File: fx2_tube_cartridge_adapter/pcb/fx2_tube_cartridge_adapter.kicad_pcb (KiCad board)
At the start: 2 copper layers, 56.5 x 53.5 mm, 3 parts

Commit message: Updated netlist as per hoglet's recommendations in http://www.stardot.org.uk/forums/viewtopic.php?f=3&t=13882&p=186963#p186908
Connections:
- CONN pad L8: (no net) -> cpu_CLK_jumper
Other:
- board text added: "- check that it's OK to have the lcsoft board below the flap in the plus 1 - consider ditching the tube interface, otherwise wire up 74hct00 and 74hct08 - check all TODO items in python netlist"
- board text added: "Electron cartridge / BBC Tube adapter for FX2 logic analyzer + decode6502 http://myelin.nz/acorn/fx2tube Copyright 2017 Google LLC Designed by Phillip Pearson"
- board text removed: "- check that it's OK to have the lcsoft board below the flap in the plus 1 - consider ditching the tube interface, otherwise wire up 74hct00 and 74hct08"
- board text removed: "Electron cartridge / BBC Tube adapter for FX2 logic analyzer + decode6502 Copyright 2017 Google LLC Designed by Phillip Pearson"
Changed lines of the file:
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@@
     (zones 0)
     (modules 3)
-    (nets 29)
+    (nets 30)
   )
   (page A4)
@@
   (net 27 cpu_nNMI)
   (net 28 cpu_SYNC)
+  (net 29 cpu_CLK_jumper)
   (net_class Default "This is the default net class."
     (clearance 0.1778)
@@
     (add_net cpu_A6)
     (add_net cpu_CLK)
+    (add_net cpu_CLK_jumper)
     (add_net cpu_D0)
     (add_net cpu_D1)
@@
     (pad L6 thru_hole circle (at 12.7 -2.54 90) (size 1.524 1.524) (drill 1.016) (layers *.Cu *.Mask)
       (net 2 GND))
-    (pad L8 thru_hole circle (at 12.7 0 90) (size 1.524 1.524) (drill 1.016) (layers *.Cu *.Mask))
+    (pad L8 thru_hole circle (at 12.7 0 90) (size 1.524 1.524) (drill 1.016) (layers *.Cu *.Mask)
+      (net 29 cpu_CLK_jumper))
     (pad L10 thru_hole circle (at 12.7 2.54 90) (size 1.524 1.524) (drill 1.016) (layers *.Cu *.Mask)
       (net 2 GND))
@@
       (net 2 GND))
   )
-  (gr_text "- check that it's OK\nto have the lcsoft\nboard below the flap\nin the plus 1\n\n- consider ditching\nthe tube interface,\notherwise wire up\n74hct00 and\n74hct08" (at 113.51 53.53) (layer F.Fab)
+  (gr_text "- check that it's OK\nto have the lcsoft\nboard below the flap\nin the plus 1\n\n- consider ditching\nthe tube interface,\notherwise wire up\n74hct00 and\n74hct08\n\n- check all TODO\nitems in python\nnetlist" (at 113.04 62.38) (layer F.Fab)
     (effects (font (size 1 1) (thickness 0.2)) (justify left))
   )
-  (gr_text "Electron cartridge / BBC Tube adapter\nfor FX2 logic analyzer + decode6502\n\nCopyright 2017 Google LLC\nDesigned by Phillip Pearson" (at 77.88 60.23) (layer B.SilkS)
+  (gr_text "Electron cartridge / BBC Tube adapter\nfor FX2 logic analyzer + decode6502\n\nhttp://myelin.nz/acorn/fx2tube\n\nCopyright 2017 Google LLC\nDesigned by Phillip Pearson" (at 77.88 60.23) (layer B.SilkS)
     (effects (font (size 1 1) (thickness 0.2)) (justify mirror))
   )

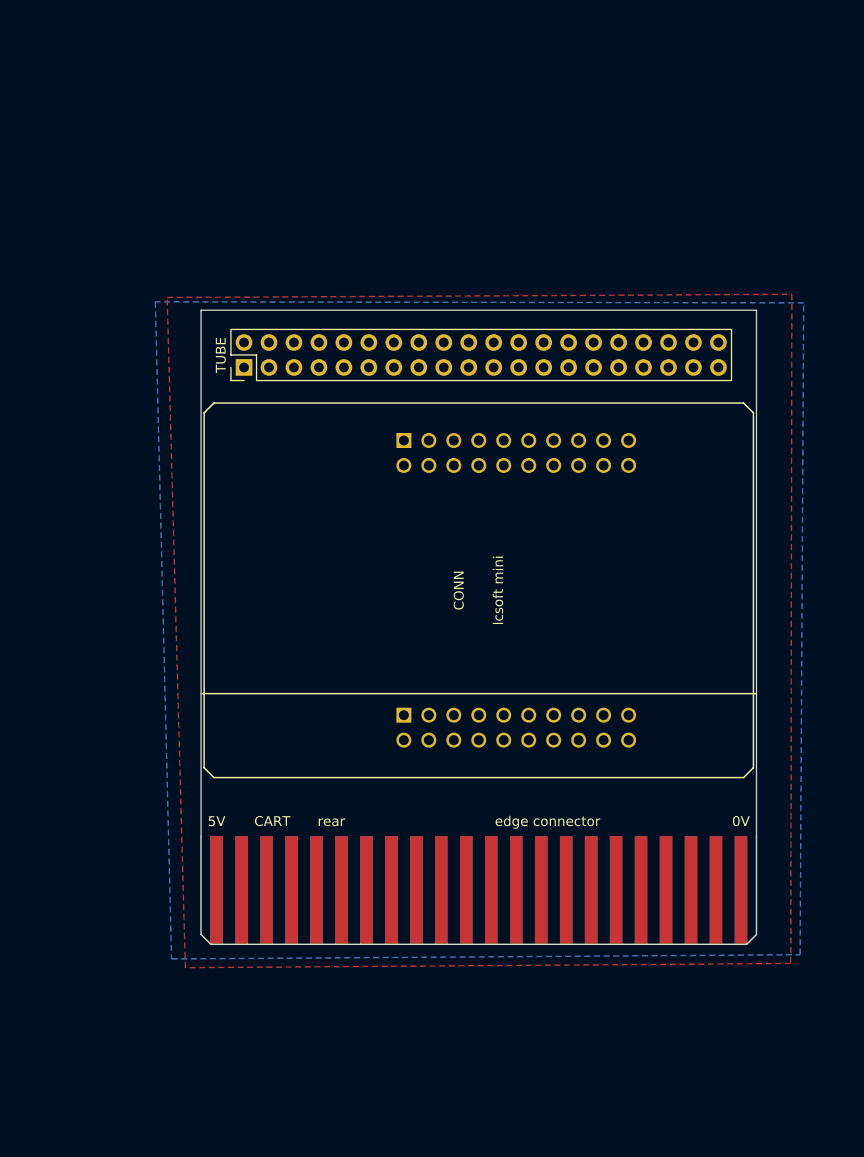
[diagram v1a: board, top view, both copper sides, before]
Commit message: fx2_tube_cartridge_adapter: routed cartridge to tube connections
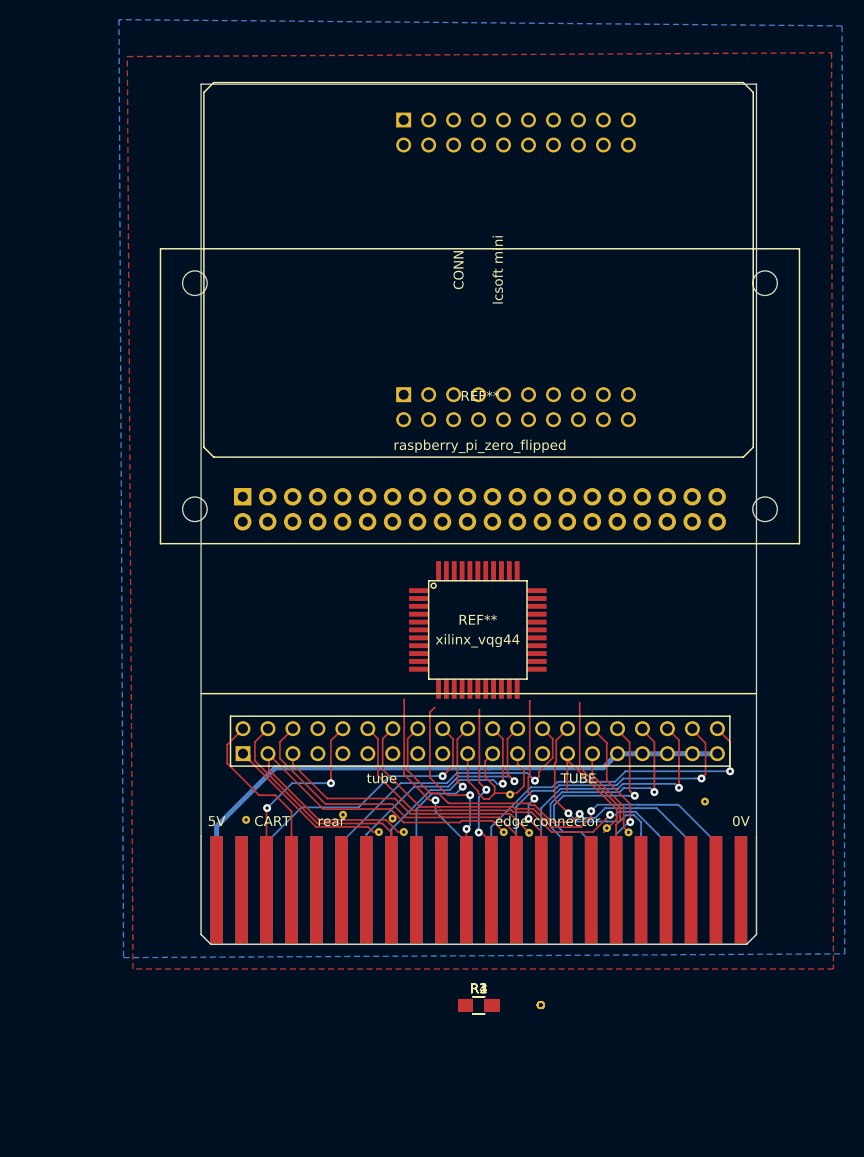
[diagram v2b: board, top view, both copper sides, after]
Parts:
- removed the TUBE at (55.1, 37.8)
- added R1, R2, R3, R4: 1k, Resistors_SMD:R_0805_HandSoldering, F.Cu at (79.0, 102.7)
- added REF**: raspberry_pi_zero_flipped, myelin-kicad:raspberry_pi_zero_flipped, F.Cu at (79.1, 55.7)
- added REF**: xilinx_vqg44, myelin-kicad:xilinx_vqg44, F.Cu at (78.9, 64.5)
- added TUBE: tube, myelin-kicad:header_2x20_100mil, F.Cu at (79.1, 75.8)
- added staple_single1: , myelin-kicad:via_single, F.Cu at (68.8, 85.1)
- added staple_single10: , myelin-kicad:via_single, F.Cu at (82.2, 81.3)
- added staple_single11: , myelin-kicad:via_single, F.Cu at (102.0, 82.0)
- added staple_single12, staple_single13, staple_single14, staple_single15, staple_single16, staple_single17, staple_single18, staple_single19, staple_single20: , myelin-kicad:via_single, F.Cu at (85.3, 102.7)
- added staple_single2: , myelin-kicad:via_single, F.Cu at (71.4, 85.1)
- added staple_single3: , myelin-kicad:via_single, F.Cu at (92.0, 84.7)
- added staple_single4: , myelin-kicad:via_single, F.Cu at (94.2, 85.1)
- added staple_single5: , myelin-kicad:via_single, F.Cu at (81.5, 85.1)
- added staple_single6: , myelin-kicad:via_single, F.Cu at (84.1, 85.2)
- added staple_single7: , myelin-kicad:via_single, F.Cu at (55.3, 83.8)
- added staple_single8: , myelin-kicad:via_single, F.Cu at (65.2, 83.3)
- added staple_single9: , myelin-kicad:via_single, F.Cu at (70.2, 83.7)
- moved CONN 32.6 mm to (79.0, 27.9)
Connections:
- CART pad B11: (no net) -> cpu_A7
- CONN pad R11: (no net) -> analyzer_PA2
- CONN pad R7: (no net) -> analyzer_PA6
- CONN pad R8: (no net) -> analyzer_PA5
- CONN pad R9: (no net) -> analyzer_PA4
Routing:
- net GND: track 0.00 -> 133.0 mm
- net 5V: track 0.00 -> 68.1 mm
- net cpu_D1: track 0.00 -> 48.6 mm, vias 0 -> 1
- net cpu_D0: track 0.00 -> 43.9 mm, vias 0 -> 1
- net cpu_D2: track 0.00 -> 42.9 mm, vias 0 -> 1
- net cpu_A6: track 0.00 -> 38.0 mm, vias 0 -> 1
- net cpu_nIRQ: track 0.00 -> 36.4 mm
- net cpu_D7: track 0.00 -> 34.3 mm, vias 0 -> 1
- net cpu_A5: track 0.00 -> 34.2 mm, vias 0 -> 1
- net cpu_D3: track 0.00 -> 31.3 mm, vias 0 -> 1
- net cpu_A4: track 0.00 -> 30.1 mm, vias 0 -> 1
- net cpu_D6: track 0.00 -> 29.4 mm, vias 0 -> 1
- net cpu_A3: track 0.00 -> 27.7 mm, vias 0 -> 1
- net cpu_A2: track 0.00 -> 27.4 mm, vias 0 -> 1
- net cpu_CLK: track 0.00 -> 26.5 mm
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- added copper zone on F.Cu, net GND
- removed copper zone on F.Cu, net 5V
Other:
- board size 56.5 x 53.5 mm -> 56.5 x 76.5 mm
- net class Clocks added: clearance 0.3302, trace_width 0.1778, via_dia 0.8128, via_drill 0.3302
- net class Data added: clearance 0.1778, trace_width 0.1778, via_dia 0.8128, via_drill 0.3302
- net class Shielded Clocks added: clearance 0.1778, trace_width 0.1778, via_dia 0.8128, via_drill 0.3302
- board text added: "- check all TODO items in python netlist"
- board text removed: "- check that it's OK to have the lcsoft board below the flap in the plus 1 - consider ditching the tube interface, otherwise wire up 74hct00 and 74hct08 - check all TODO items in python netlist"

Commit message: fx2_tube_cartridge_adapter: Added CPLD and Pi Zero to netlist, and enlarged the PCB a bit to fit them
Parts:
- removed REF**: raspberry_pi_zero_flipped, myelin-kicad:raspberry_pi_zero_flipped
- removed REF**: xilinx_vqg44, myelin-kicad:xilinx_vqg44
- added C1: 100n, Capacitors_SMD:C_0805_HandSoldering, F.Cu at (94.4, 105.4)
- added C2: 100n, Capacitors_SMD:C_0805_HandSoldering, F.Cu at (87.2, 105.6)
- added C3: 1u, Capacitors_SMD:C_0805_HandSoldering, F.Cu at (80.7, 106.0)
- added C4: 1u, Capacitors_SMD:C_0805_HandSoldering, F.Cu at (73.1, 105.6)
- added C5: 1u, Capacitors_SMD:C_0805_HandSoldering, F.Cu at (67.0, 105.3)
- added FX2PWR: Power from FX2, Pin_Headers:Pin_Header_Straight_1x02_Pitch2.54mm, F.Cu at (101.2, 14.9)
- added JTAG1: jtag, Pin_Headers:Pin_Header_Straight_2x05_Pitch2.54mm, F.Cu at (100.4, 59.0)
- added PI1: Raspberry Pi Zero, myelin-kicad:raspberry_pi_zero_flipped, F.Cu at (79.1, 55.8)
- added PIPWR: Power from Pi, Pin_Headers:Pin_Header_Straight_1x02_Pitch2.54mm, F.Cu at (101.8, 20.2)
- added PL1: XC9572XL, myelin-kicad:xilinx_vqg44, F.Cu at (78.7, 64.3)
- added SERIAL1: Pi Serial, Pin_Headers:Pin_Header_Straight_1x03_Pitch2.54mm, F.Cu at (55.3, 59.9)
- added U1: MCP1700T-3302E/MB, TO_SOT_Packages_SMD:SOT-89-3, F.Cu at (63.3, 63.1)
- CONN: moved to B.Cu
- moved R1 74.2 mm to (93.2, 29.8)
- moved R2 72.0 mm to (93.2, 32.1)
- moved R4 69.9 mm to (93.2, 34.3)
- moved R3 67.8 mm to (93.2, 36.4)
- moved staple_single12 13.0 mm to (85.3, 115.7)
- moved staple_single13 13.0 mm to (85.3, 115.7)
- moved staple_single14 13.0 mm to (85.3, 115.7)
- moved staple_single15 13.0 mm to (85.3, 115.7)
- moved staple_single16 13.0 mm to (85.3, 115.7)
- moved staple_single17 13.0 mm to (85.3, 115.7)
- moved staple_single18 13.0 mm to (85.3, 115.7)
- moved staple_single19 13.0 mm to (85.3, 115.7)
- moved staple_single20 13.0 mm to (85.3, 115.7)
- moved CONN 1.27 mm to (78.9, 29.2)
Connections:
- CONN pad L19: 3V3 -> 3V3_FX2
- CONN pad L20: 3V3 -> 3V3_FX2
- TUBE pad 8: tube_nTUBE -> bbc_nTUBE
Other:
- board size 56.5 x 76.5 mm -> 66.5 x 76.5 mm

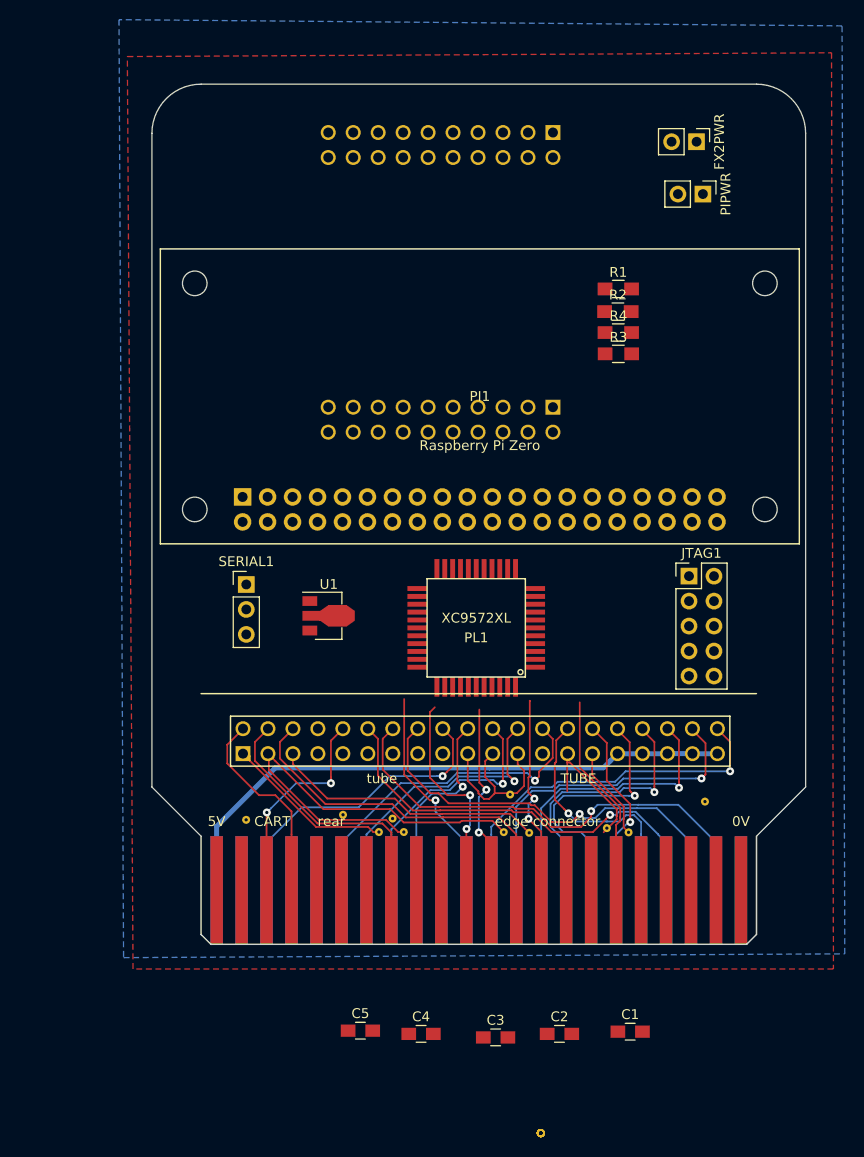
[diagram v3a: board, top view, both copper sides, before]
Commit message: fx2_tube_cartridge_adapter: Routed CPLD and most other signals
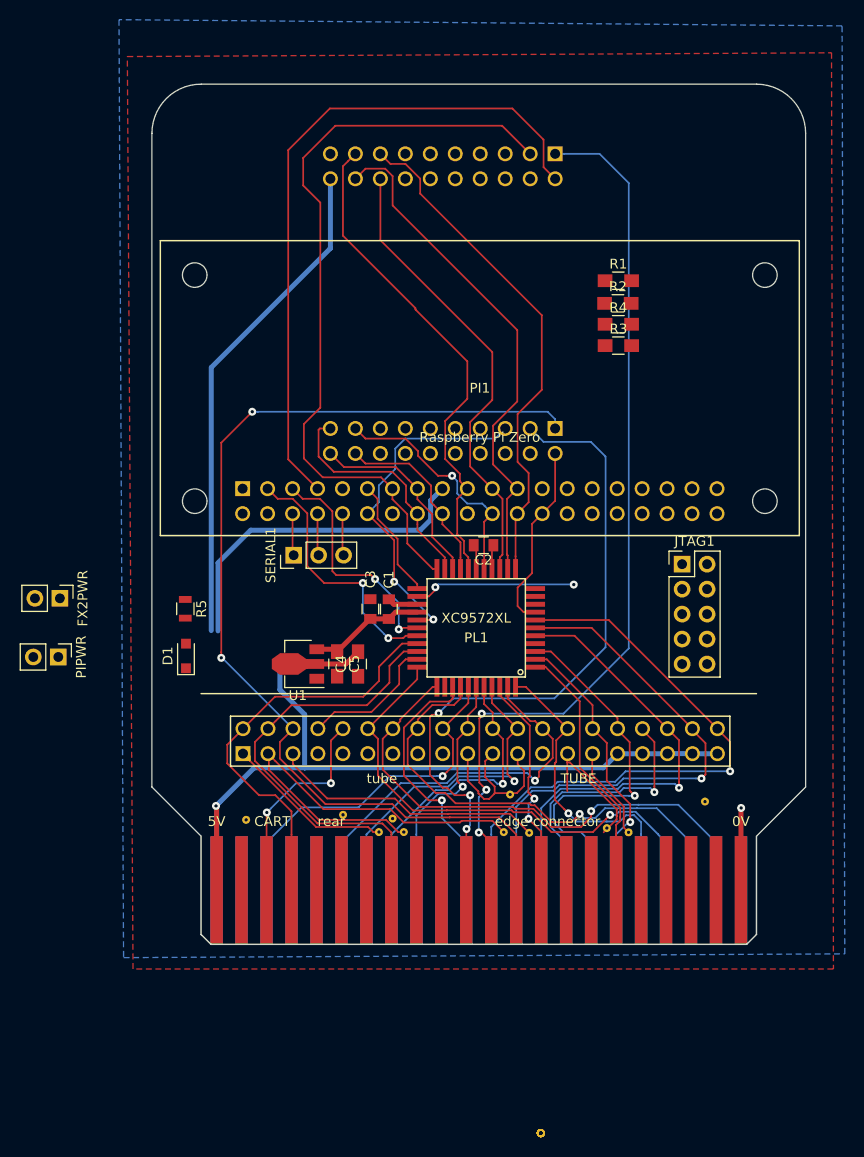
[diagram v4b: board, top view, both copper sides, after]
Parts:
- added D1: BAT54, Diodes_SMD:D_SOD-323_HandSoldering, F.Cu at (49.2, 67.2)
- added R5: 10k, Resistors_SMD:R_0805, F.Cu at (49.1, 62.4)
- C1, C2, C3: footprint Capacitors_SMD:C_0805_HandSoldering -> Capacitors_SMD:C_0805
- moved PIPWR 80.7 mm to (36.2, 67.3)
- moved FX2PWR 79.7 mm to (36.4, 61.3)
- moved C2 50.3 mm to (79.5, 55.9), turned to 180 degrees
- moved C1 49.5 mm to (69.9, 62.4), turned to 90 degrees
- moved C3 45.4 mm to (68.0, 62.4), turned to 90 degrees
- moved C4 38.2 mm to (66.7, 68.0), turned to 90 degrees
- moved C5 37.4 mm to (64.6, 68.0), turned to 270 degrees
- moved SERIAL1 5.66 mm to (60.2, 56.9), turned to 90 degrees
- moved U1 5.40 mm to (61.0, 68.0), turned to 180 degrees
- moved CONN 2.18 mm to (79.1, 31.3)
- moved JTAG1 1.41 mm to (99.7, 57.8)
- moved PI1 0.84 mm to (79.1, 54.9)
- moved R2 0.84 mm to (93.2, 31.3)
- moved R3 0.84 mm to (93.2, 35.6)
- moved R4 0.84 mm to (93.2, 33.4)
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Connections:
- CONN pad L15: cpu_D0 -> tube_D0
- CONN pad L16: cpu_D1 -> tube_D1
- CONN pad L17: cpu_D2 -> tube_D2
- CONN pad L18: cpu_D3 -> tube_D3
- CONN pad L2: cpu_nRST -> tube_nRST
- CONN pad L3: cpu_A0 -> tube_A0
- CONN pad R17: cpu_D7 -> tube_D7
- CONN pad R18: cpu_D6 -> tube_D6
- CONN pad R19: cpu_D5 -> tube_D5
- CONN pad R2: cpu_CLK -> tube_CLK
- CONN pad R20: cpu_D4 -> tube_D4
- CONN pad R5: cpu_RnW -> tube_RnW
- PI1 pad 26: tube_PHI0 -> tube_CLK
- PL1 pad 1: cpu_CLK -> elk_16MHz
- PL1 pad 12: cpu_A2 -> tube_D0
- PL1 pad 13: cpu_A1 -> tube_D3
- PL1 pad 14: cpu_A0 -> tube_D1
- PL1 pad 16: cpu_D0 -> tube_D7
- PL1 pad 18: cpu_D2 -> tube_D2
- PL1 pad 19: cpu_D1 -> tube_D6
- PL1 pad 2: cpu_D4 -> cpu_A1
- PL1 pad 20: tube_CLK -> tube_D4
- PL1 pad 21: tube_D3 -> tube_D5
- PL1 pad 22: tube_D0 -> tube_A0
- PL1 pad 23: tube_D1 -> tube_nTUBE
- PL1 pad 27: tube_D7 -> tube_RnW
- PL1 pad 28: tube_D2 -> tube_A2
- PL1 pad 29: tube_D6 -> tube_A1
- PL1 pad 3: cpu_A7 -> cpu_A2
- PL1 pad 30: tube_D4 -> cpu_RnW
- PL1 pad 31: tube_D5 -> cpu_CLK
- PL1 pad 32: tube_A0 -> bbc_nTUBE
- PL1 pad 33: tube_nTUBE -> cpu_D0
- PL1 pad 34: tube_RnW -> cpu_D1
- PL1 pad 36: bbc_nTUBE -> cpu_A7
- PL1 pad 37: tube_A2 -> cpu_D2
- PL1 pad 38: tube_A1 -> cpu_D3
- PL1 pad 39: cpu_D3 -> cpu_D4
- PL1 pad 41: cpu_RnW -> cpu_D6
- PL1 pad 42: cpu_D7 -> elk_nINFC
- PL1 pad 43: cpu_D6 -> cpu_D7
- PL1 pad 44: elk_16MHz -> cpu_A0
- PL1 pad 5: cpu_A6 -> cpu_A4
- PL1 pad 7: cpu_A4 -> cpu_A6
- PL1 pad 8: elk_nINFC -> tube_CLK
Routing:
- net tube_A0: track 0.00 -> 78.2 mm
- net cpu_nNMI: track 19.7 -> 93.1 mm, vias 2 -> 3
- net tube_nRST: track 0.00 -> 69.2 mm
- net cpu_nIRQ: track 36.4 -> 105.1 mm, vias 0 -> 2
- net tube_D3: track 0.00 -> 52.2 mm
- net tube_D0: track 0.00 -> 52.0 mm
- net 3V3_FX2: track 0.00 -> 51.0 mm
- net tube_D2: track 0.00 -> 50.8 mm
- net cpu_READY: track 22.0 -> 69.7 mm, vias 2 -> 3
- net tube_D1: track 0.00 -> 46.8 mm
- net tube_RnW: track 0.00 -> 35.1 mm, vias 0 -> 2
- net 3V3_PI: track 0.00 -> 34.0 mm
- net tube_A1: track 0.00 -> 26.5 mm, vias 0 -> 2
- net 5V: track 68.1 -> 94.3 mm, vias 0 -> 1
- net tube_D7: track 0.00 -> 24.5 mm, vias 0 -> 1
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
